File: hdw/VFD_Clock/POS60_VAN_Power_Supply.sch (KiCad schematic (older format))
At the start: 28 parts

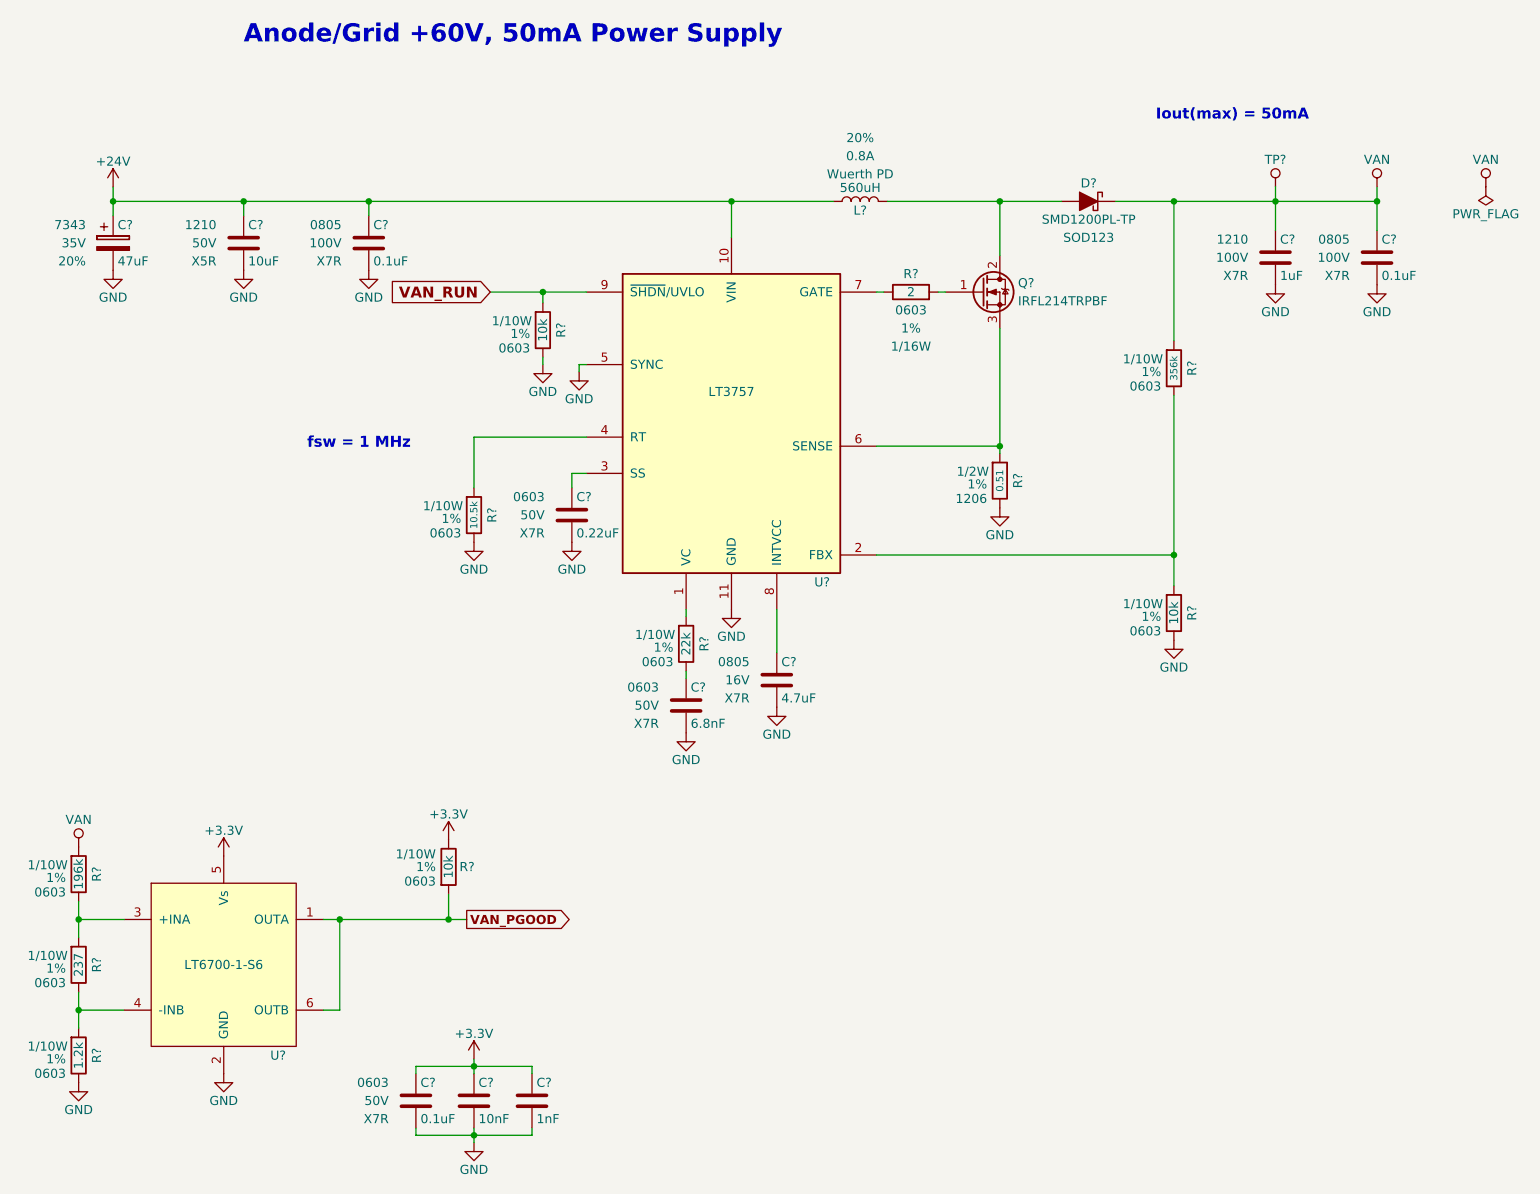
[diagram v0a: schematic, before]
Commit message: Redesigned +1.2V VFF
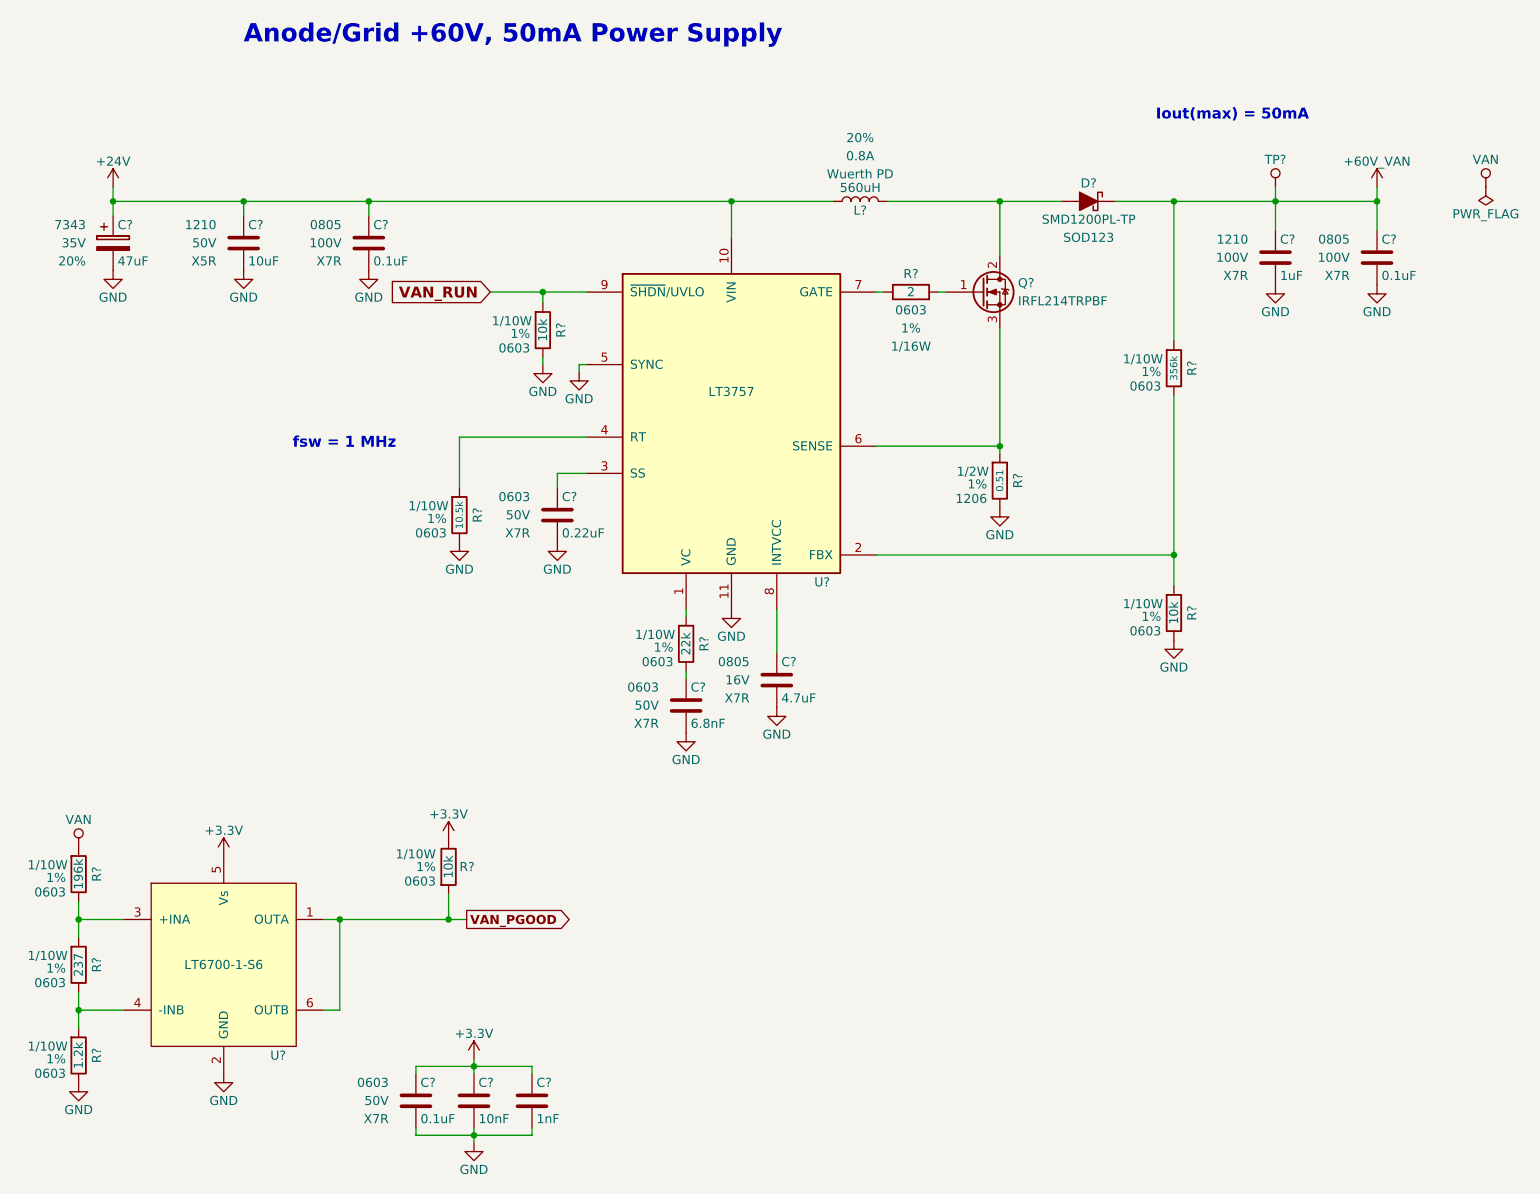
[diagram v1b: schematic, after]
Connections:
- net VAN: no longer C?.1, C?.1, D?.1 (K), R?.1, TP?.1 (TP)
- new net +60V_VAN: C?.1, C?.1, D?.1 (K), R?.1, TP?.1 (TP)
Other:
- moved on the sheet: C?, R?
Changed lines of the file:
@@
 $Descr A 11000 8500
 encoding utf-8
-Sheet 4 14
+Sheet 4 13
 Title ""
 Date ""
@@
 L power:GND #PWR?
 U 1 1 5A0BD101
-P 4770 3800
-F 0 "#PWR?" H 4770 3550 50  0001 C CNN
-F 1 "GND" H 4770 3650 50  0000 C CNN
-F 2 "" H 4770 3800 50  0001 C CNN
-F 3 "" H 4770 3800 50  0001 C CNN
-	1    4770 3800
+P 4690 3800
+F 0 "#PWR?" H 4690 3550 50  0001 C CNN
+F 1 "GND" H 4690 3650 50  0000 C CNN
+F 2 "" H 4690 3800 50  0001 C CNN
+F 3 "" H 4690 3800 50  0001 C CNN
+	1    4690 3800
 	1    0    0    -1
 $EndComp
@@
 L power:GND #PWR?
 U 1 1 5A0BD107
-P 4230 3800
-F 0 "#PWR?" H 4230 3550 50  0001 C CNN
-F 1 "GND" H 4230 3650 50  0000 C CNN
-F 2 "" H 4230 3800 50  0001 C CNN
-F 3 "" H 4230 3800 50  0001 C CNN
-	1    4230 3800
+P 4150 3800
+F 0 "#PWR?" H 4150 3550 50  0001 C CNN
+F 1 "GND" H 4150 3650 50  0000 C CNN
+F 2 "" H 4150 3800 50  0001 C CNN
+F 3 "" H 4150 3800 50  0001 C CNN
+	1    4150 3800
 	1    0    0    -1
 $EndComp
@@
 L Custom_Library:C_Custom C?
 U 1 1 5A174B40
-P 4770 3650
-F 0 "C?" H 4795 3750 50  0000 L CNN
-F 1 "0.22uF" H 4795 3550 50  0000 L CNN
-F 2 "Capacitors_SMD:C_0603" H 4808 3500 50  0001 C CNN
-F 3 "" H 4795 3750 50  0001 C CNN
-F 4 "0603" H 4620 3750 50  0000 R CNN "display_footprint"
-F 5 "50V" H 4620 3650 50  0000 R CNN "Voltage"
-F 6 "X7R" H 4620 3550 50  0000 R CNN "Dielectric"
-F 7 "490-5402-1-ND" H 0   0   50  0001 C CNN "Digi-Key PN"
-	1    4770 3650
+P 4690 3650
+F 0 "C?" H 4715 3750 50  0000 L CNN
+F 1 "0.22uF" H 4715 3550 50  0000 L CNN
+F 2 "Capacitors_SMD:C_0603" H 4728 3500 50  0001 C CNN
+F 3 "" H 4715 3750 50  0001 C CNN
+F 4 "0603" H 4540 3750 50  0000 R CNN "display_footprint"
+F 5 "50V" H 4540 3650 50  0000 R CNN "Voltage"
+F 6 "X7R" H 4540 3550 50  0000 R CNN "Dielectric"
+F 7 "490-5402-1-ND" H -80 0   50  0001 C CNN "Digi-Key PN"
+	1    4690 3650
 	1    0    0    -1
 $EndComp
@@
 L Custom_Library:R_Custom R?
 U 1 1 5A176CF5
-P 4230 3650
-F 0 "R?" V 4130 3650 50  0000 C CNN
-F 1 "10.5k" V 4230 3650 40  0000 C CNN
-F 2 "Resistors_SMD:R_0603" H 4230 3650 50  0001 C CNN
-F 3 "" H 4230 3650 50  0001 C CNN
-F 4 "0603" H 4300 3550 50  0000 L CNN "display_footprint"
-F 5 "1%" H 4300 3630 50  0000 L CNN "Tolerance"
-F 6 "1/10W" H 4290 3700 50  0000 L CNN "Wattage"
-F 7 "P10.5KHCT-ND" H 0   0   50  0001 C CNN "Digi-Key PN"
-	1    4230 3650
+P 4150 3650
+F 0 "R?" V 4050 3650 50  0000 C CNN
+F 1 "10.5k" V 4150 3650 40  0000 C CNN
+F 2 "Resistors_SMD:R_0603" H 4150 3650 50  0001 C CNN
+F 3 "" H 4150 3650 50  0001 C CNN
+F 4 "0603" H 4220 3550 50  0000 L CNN "display_footprint"
+F 5 "1%" H 4220 3630 50  0000 L CNN "Tolerance"
+F 6 "1/10W" H 4210 3700 50  0000 L CNN "Wattage"
+F 7 "P10.5KHCT-ND" H -80 0   50  0001 C CNN "Digi-Key PN"
+	1    4150 3650
 	-1   0    0    -1
 $EndComp
@@
 $EndComp
 $Comp
-L Custom_Library:VAN #PWR?
-U 1 1 5A49F951
-P 9210 1840
-F 0 "#PWR?" H 9210 1690 50  0001 C CNN
-F 1 "VAN" H 9210 1990 50  0000 C CNN
-F 2 "" H 9210 1840 50  0001 C CNN
-F 3 "" H 9210 1840 50  0001 C CNN
-	1    9210 1840
-	1    0    0    -1
-$EndComp
-$Comp
 L Custom_Library:LT6700-1-S6 U?
 U 1 1 5A4ABE2A
@@
 	1    0    0    -1
 $EndComp
-Text Notes 3310 3290 0    60   ~ 12
+Text Notes 3230 3290 0    60   ~ 12
 fsw = 1 MHz
 Text Notes 7990 1480 0    60   ~ 12
@@
 Connection ~ 7130 1920
 Wire Wire Line
-	4230 3500 4230 3220
-Wire Wire Line
-	4230 3220 4850 3220
-Wire Wire Line
-	4770 3500 4770 3420
-Wire Wire Line
-	4770 3420 4850 3420
+	4150 3500 4150 3220
+Wire Wire Line
+	4690 3500 4690 3420
 Wire Wire Line
 	8090 2990 8090 3870
@@
 Wire Wire Line
 	2050 6380 2300 6380
+$Comp
+L Custom_Library:+60V_VAN #PWR?
+U 1 1 5CB134C0
+P 9210 1840
+F 0 "#PWR?" H 9210 1690 50  0001 C CNN
+F 1 "+60V_VAN" H 9210 1980 50  0000 C CNN
+F 2 "" H 9210 1840 50  0000 C CNN
+F 3 "" H 9210 1840 50  0000 C CNN
+	1    9210 1840
+	1    0    0    -1
+$EndComp
+Wire Wire Line
+	4150 3220 4850 3220
+Wire Wire Line
+	4690 3420 4850 3420
 $EndSCHEMATC
